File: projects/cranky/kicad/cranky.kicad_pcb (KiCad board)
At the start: 2 copper layers, 50 x 50 mm, 50 parts, among them CON1 USB-MINI-B, P1 ISP, P2 CONN_01X04, P3 CONN_01X04, P4 CONN_01X04, P5 CONN_01X04, Q1 2N7002P, Q2 2N7002P, Q3 ISL9V3040D3ST, Q4 ISL9V3040D3ST, Q5 VND5N07, Q6 VND5N07, SW1 SW_PUSH_SMALL, SW2 SW_PUSH_SMALL, U1 ATMEGA32U4-A, U2 LTV-826S, U3 LM7805CT, X1 16MHz

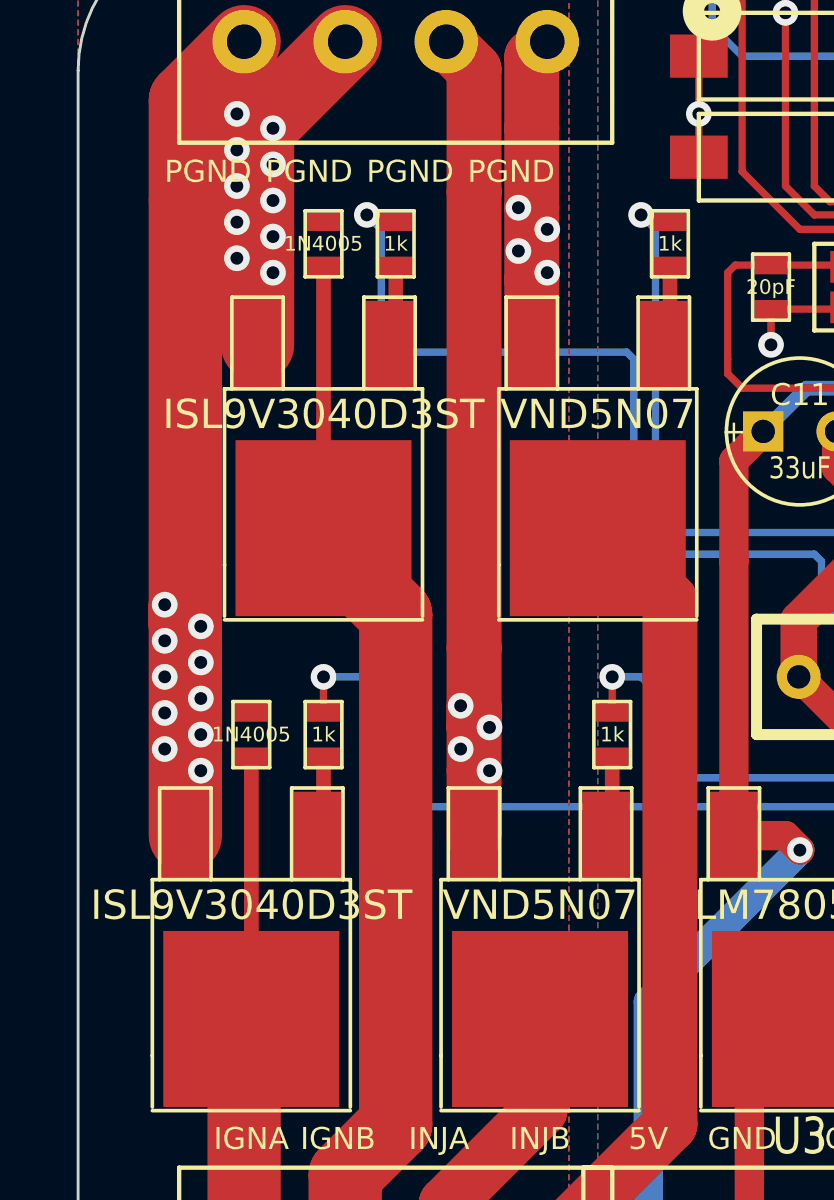
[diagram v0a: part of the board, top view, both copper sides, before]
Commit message: finished rerouting
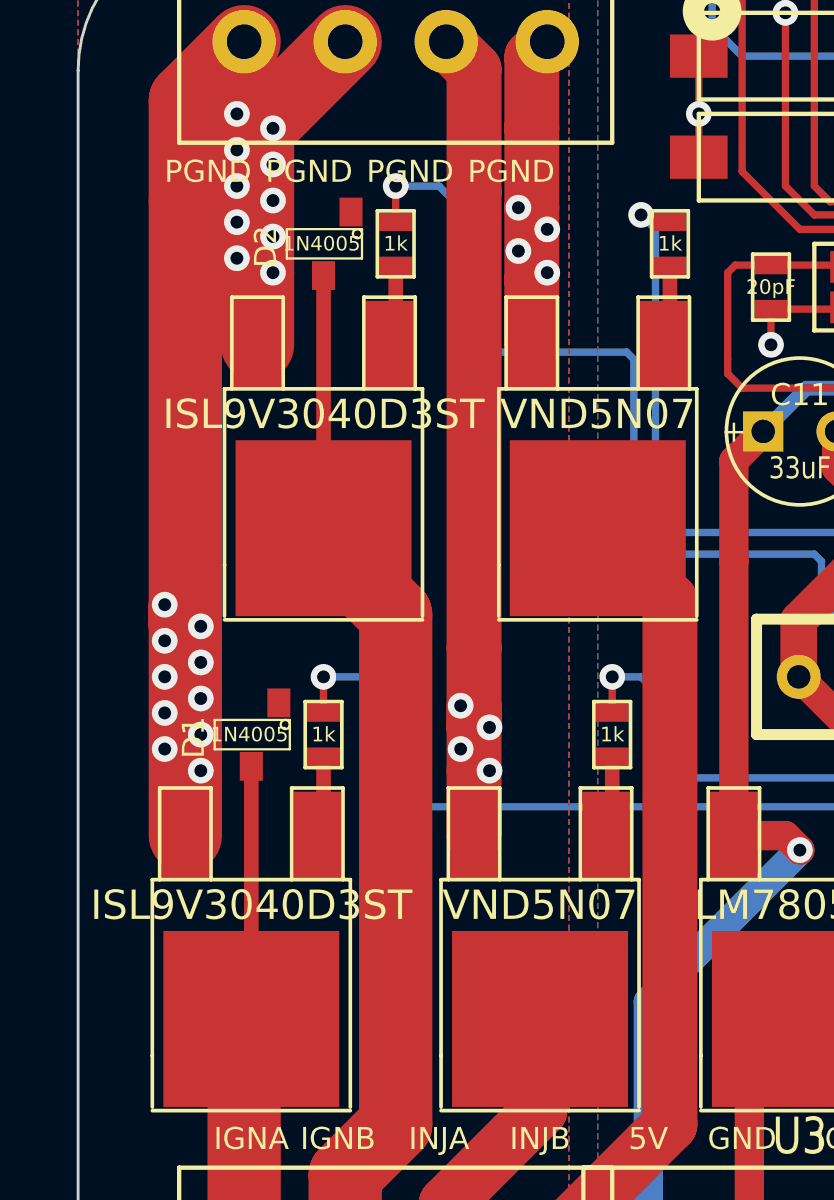
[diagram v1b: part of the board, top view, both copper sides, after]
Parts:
- D1, D2: footprint SM0603_VALUE -> SOT23
- turned D1 to 180 degrees
- turned D2 to 180 degrees
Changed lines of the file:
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@@
     (thickness 1.6)
     (drawings 27)
-    (tracks 482)
+    (tracks 483)
     (zones 0)
     (modules 50)
@@
     (19 F.Paste user)
     (20 B.SilkS user)
-    (21 F.SilkS user hide)
+    (21 F.SilkS user)
     (22 B.Mask user)
     (23 F.Mask user)
@@
     (mod_text_size 1 1)
     (mod_text_width 0.15)
-    (pad_size 6.096 6.096)
+    (pad_size 0.8001 1.00076)
     (pad_drill 0)
     (pad_to_mask_clearance 0)
@@
   )
   (module SM0603_VALUE (layer F.Cu)
-    (at 51 98 270)
-    (attr smd)
-    (fp_text reference D1 (at 0 0 270) (layer F.SilkS) hide
-      (effects (font (size 0.508 0.508) (thickness 0.1143)))
-    )
-    (fp_text value 1N4005 (at 0 0 360) (layer F.SilkS)
-      (effects (font (size 0.508 0.508) (thickness 0.1143)))
-    )
-    (fp_line (start -1.143 -0.635) (end 1.143 -0.635) (layer F.SilkS) (width 0.127))
-    (fp_line (start 1.143 -0.635) (end 1.143 0.635) (layer F.SilkS) (width 0.127))
-    (fp_line (start 1.143 0.635) (end -1.143 0.635) (layer F.SilkS) (width 0.127))
-    (fp_line (start -1.143 0.635) (end -1.143 -0.635) (layer F.SilkS) (width 0.127))
-    (pad 1 smd rect (at -0.762 0 270) (size 0.635 1.143)
-      (layers F.Cu F.Paste F.Mask)
-      (net 35 GNDPWR)
-    )
-    (pad 2 smd rect (at 0.762 0 270) (size 0.635 1.143)
-      (layers F.Cu F.Paste F.Mask)
-      (net 10 /IGNA)
-    )
-    (model smd\resistors\R0603.wrl
-      (at (xyz 0 0 0.001))
-      (scale (xyz 0.5 0.5 0.5))
-      (rotate (xyz 0 0 0))
-    )
-  )
-  (module SM0603_VALUE (layer F.Cu)
-    (at 53.5 81 270)
-    (attr smd)
-    (fp_text reference D2 (at 0 0 270) (layer F.SilkS) hide
-      (effects (font (size 0.508 0.508) (thickness 0.1143)))
-    )
-    (fp_text value 1N4005 (at 0 0 360) (layer F.SilkS)
-      (effects (font (size 0.508 0.508) (thickness 0.1143)))
-    )
-    (fp_line (start -1.143 -0.635) (end 1.143 -0.635) (layer F.SilkS) (width 0.127))
-    (fp_line (start 1.143 -0.635) (end 1.143 0.635) (layer F.SilkS) (width 0.127))
-    (fp_line (start 1.143 0.635) (end -1.143 0.635) (layer F.SilkS) (width 0.127))
-    (fp_line (start -1.143 0.635) (end -1.143 -0.635) (layer F.SilkS) (width 0.127))
-    (pad 1 smd rect (at -0.762 0 270) (size 0.635 1.143)
-      (layers F.Cu F.Paste F.Mask)
-      (net 35 GNDPWR)
-    )
-    (pad 2 smd rect (at 0.762 0 270) (size 0.635 1.143)
-      (layers F.Cu F.Paste F.Mask)
-      (net 11 /IGNB)
-    )
-    (model smd\resistors\R0603.wrl
-      (at (xyz 0 0 0.001))
-      (scale (xyz 0.5 0.5 0.5))
-      (rotate (xyz 0 0 0))
-    )
-  )
-  (module SM0603_VALUE (layer F.Cu)
     (at 53.5 98 90)
     (attr smd)
@@
       (scale (xyz 0.5 0.5 0.5))
       (rotate (xyz 0 0 0))
+    )
+  )
+  (module SOT23 (layer F.Cu)
+    (at 51 98 180)
+    (tags SOT23)
+    (fp_text reference D1 (at 1.99898 -0.09906 270) (layer F.SilkS)
+      (effects (font (size 0.762 0.762) (thickness 0.11938)))
+    )
+    (fp_text value 1N4005 (at 0.0635 0 180) (layer F.SilkS)
+      (effects (font (size 0.50038 0.50038) (thickness 0.09906)))
+    )
+    (fp_circle (center -1.17602 0.35052) (end -1.30048 0.44958) (layer F.SilkS) (width 0.07874))
+    (fp_line (start 1.27 -0.508) (end 1.27 0.508) (layer F.SilkS) (width 0.07874))
+    (fp_line (start -1.3335 -0.508) (end -1.3335 0.508) (layer F.SilkS) (width 0.07874))
+    (fp_line (start 1.27 0.508) (end -1.3335 0.508) (layer F.SilkS) (width 0.07874))
+    (fp_line (start -1.3335 -0.508) (end 1.27 -0.508) (layer F.SilkS) (width 0.07874))
+    (pad 2 smd rect (at 0 -1.09982 180) (size 0.8001 1.00076)
+      (layers F.Cu F.Paste F.Mask)
+      (net 10 /IGNA)
+    )
+    (pad 1 smd rect (at -0.9525 1.09982 180) (size 0.8001 1.00076)
+      (layers F.Cu F.Paste F.Mask)
+      (net 35 GNDPWR)
+    )
+    (model smd\SOT23_3.wrl
+      (at (xyz 0 0 0))
+      (scale (xyz 0.4 0.4 0.4))
+      (rotate (xyz 0 0 180))
+    )
+  )
+  (module SOT23 (layer F.Cu)
+    (at 53.5 81 180)
+    (tags SOT23)
+    (fp_text reference D2 (at 1.99898 -0.09906 270) (layer F.SilkS)
+      (effects (font (size 0.762 0.762) (thickness 0.11938)))
+    )
+    (fp_text value 1N4005 (at 0.0635 0 180) (layer F.SilkS)
+      (effects (font (size 0.50038 0.50038) (thickness 0.09906)))
+    )
+    (fp_circle (center -1.17602 0.35052) (end -1.30048 0.44958) (layer F.SilkS) (width 0.07874))
+    (fp_line (start 1.27 -0.508) (end 1.27 0.508) (layer F.SilkS) (width 0.07874))
+    (fp_line (start -1.3335 -0.508) (end -1.3335 0.508) (layer F.SilkS) (width 0.07874))
+    (fp_line (start 1.27 0.508) (end -1.3335 0.508) (layer F.SilkS) (width 0.07874))
+    (fp_line (start -1.3335 -0.508) (end 1.27 -0.508) (layer F.SilkS) (width 0.07874))
+    (pad 2 smd rect (at 0 -1.09982 180) (size 0.8001 1.00076)
+      (layers F.Cu F.Paste F.Mask)
+      (net 11 /IGNB)
+    )
+    (pad 1 smd rect (at -0.9525 1.09982 180) (size 0.8001 1.00076)
+      (layers F.Cu F.Paste F.Mask)
+      (net 35 GNDPWR)
+    )
+    (model smd\SOT23_3.wrl
+      (at (xyz 0 0 0))
+      (scale (xyz 0.4 0.4 0.4))
+      (rotate (xyz 0 0 180))
     )
   )
@@
   (segment (start 86.5 109.84982) (end 86.5 115.75) (width 0.254) (layer F.Cu) (net 9))
   (segment (start 86.5 115.75) (end 85.75 116.5) (width 0.254) (layer F.Cu) (net 9))
-  (segment (start 51 98.762) (end 51 107.85) (width 0.508) (layer F.Cu) (net 10))
+  (segment (start 51 99) (end 51 107.85) (width 0.508) (layer F.Cu) (net 10))
   (segment (start 50.75 116.5) (end 50.75 108.1) (width 2.54) (layer F.Cu) (net 10))
   (segment (start 50.75 108.1) (end 51 107.85) (width 2.54) (layer F.Cu) (net 10))
-  (segment (start 53.5 81.762) (end 53.5 90.85) (width 0.508) (layer F.Cu) (net 11))
+  (segment (start 53.5 82) (end 53.5 90.85) (width 0.508) (layer F.Cu) (net 11))
   (segment (start 54.25 116.5) (end 54.25 113.25) (width 2.54) (layer F.Cu) (net 11))
   (segment (start 56 93.85) (end 53 90.85) (width 2.54) (layer F.Cu) (net 11))
@@
   (segment (start 56 100.5) (end 55.5 100) (width 0.254) (layer B.Cu) (net 19))
   (segment (start 82 100.5) (end 56 100.5) (width 0.254) (layer B.Cu) (net 19))
+  (segment (start 57.5 79) (end 56 79) (width 0.254) (layer B.Cu) (net 20))
+  (segment (start 56 79) (end 56 80.238) (width 0.254) (layer F.Cu) (net 20))
+  (via (at 56 79) (size 0.889) (layers F.Cu B.Cu) (net 20))
+  (segment (start 58.5 84.75) (end 58.25 84.75) (width 0.254) (layer B.Cu) (net 20))
+  (segment (start 58 79.5) (end 57.5 79) (width 0.254) (layer B.Cu) (net 20))
+  (segment (start 58 84.5) (end 58 79.5) (width 0.254) (layer B.Cu) (net 20))
+  (segment (start 58.25 84.75) (end 58 84.5) (width 0.254) (layer B.Cu) (net 20))
   (segment (start 85.8001 94.715) (end 85.8001 91.8001) (width 0.254) (layer F.Cu) (net 20))
   (segment (start 85.5 91.5) (end 82 91.5) (width 0.254) (layer B.Cu) (net 20))
   (via (at 85.5 91.5) (size 0.889) (layers F.Cu B.Cu) (net 20))
   (segment (start 85.8001 91.8001) (end 85.5 91.5) (width 0.254) (layer F.Cu) (net 20))
-  (segment (start 55.5 80.5) (end 55.5 84.5) (width 0.254) (layer B.Cu) (net 20))
   (segment (start 70.75 93.5) (end 71.25 94) (width 0.254) (layer B.Cu) (net 20))
   (segment (start 70.75 92) (end 70.75 93.5) (width 0.254) (layer B.Cu) (net 20))
@@
   (segment (start 64.25 85) (end 64.25 90.75) (width 0.254) (layer B.Cu) (net 20))
   (segment (start 64 84.75) (end 64.25 85) (width 0.254) (layer B.Cu) (net 20))
-  (segment (start 55.75 84.75) (end 64 84.75) (width 0.254) (layer B.Cu) (net 20))
-  (segment (start 55.5 84.5) (end 55.75 84.75) (width 0.254) (layer B.Cu) (net 20))
+  (segment (start 58.5 84.75) (end 64 84.75) (width 0.254) (layer B.Cu) (net 20))
   (segment (start 79.5 94) (end 71.25 94) (width 0.254) (layer B.Cu) (net 20))
   (segment (start 80.5 93) (end 79.5 94) (width 0.254) (layer B.Cu) (net 20))
   (segment (start 82 91.5) (end 80.5 93) (width 0.254) (layer B.Cu) (net 20))
-  (segment (start 55.238 80.238) (end 56 80.238) (width 0.254) (layer F.Cu) (net 20))
-  (segment (start 55 80) (end 55.238 80.238) (width 0.254) (layer F.Cu) (net 20))
-  (via (at 55 80) (size 0.889) (layers F.Cu B.Cu) (net 20))
-  (segment (start 55.5 80.5) (end 55 80) (width 0.254) (layer B.Cu) (net 20))
   (segment (start 87.262 105.25) (end 87.262 104.488) (width 0.254) (layer F.Cu) (net 21))
   (segment (start 87.5 96.25) (end 87.4003 96.1503) (width 0.254) (layer F.Cu) (net 21))

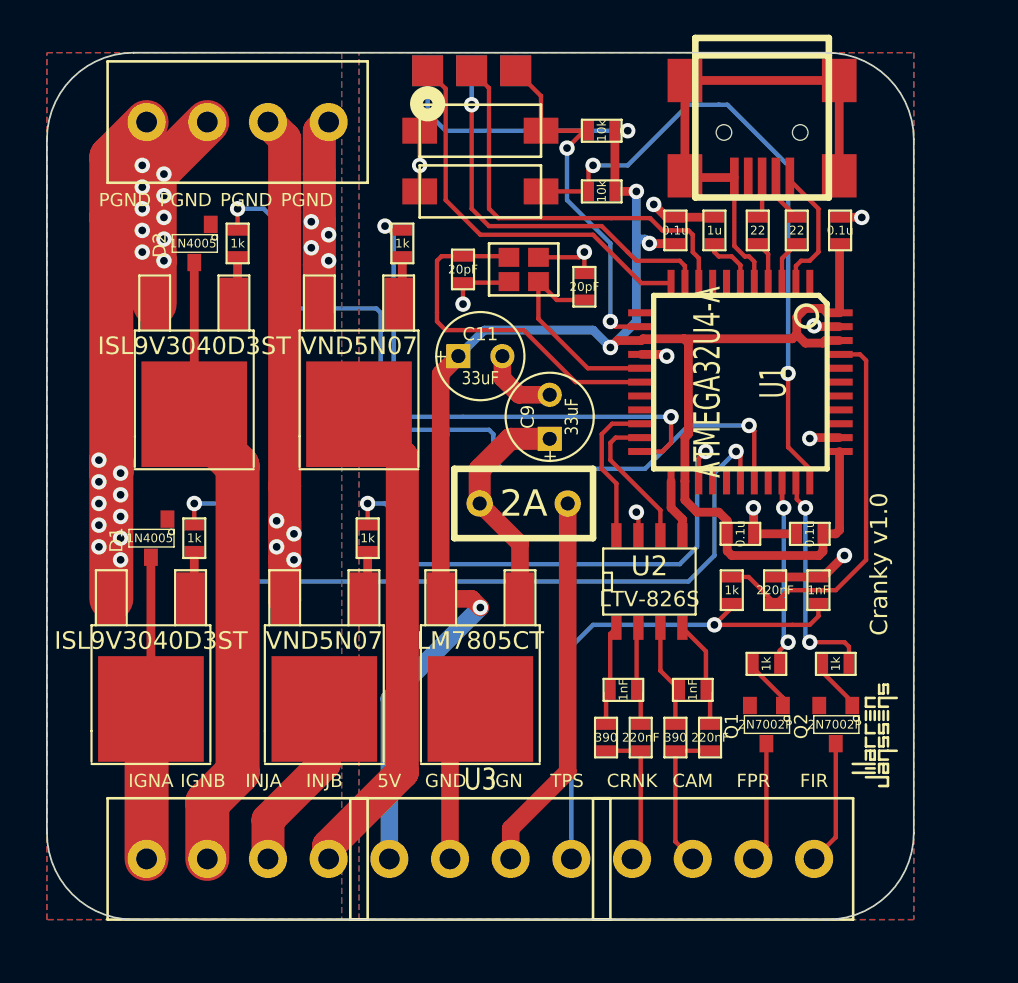
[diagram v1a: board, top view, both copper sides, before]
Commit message: adding zones for igbts
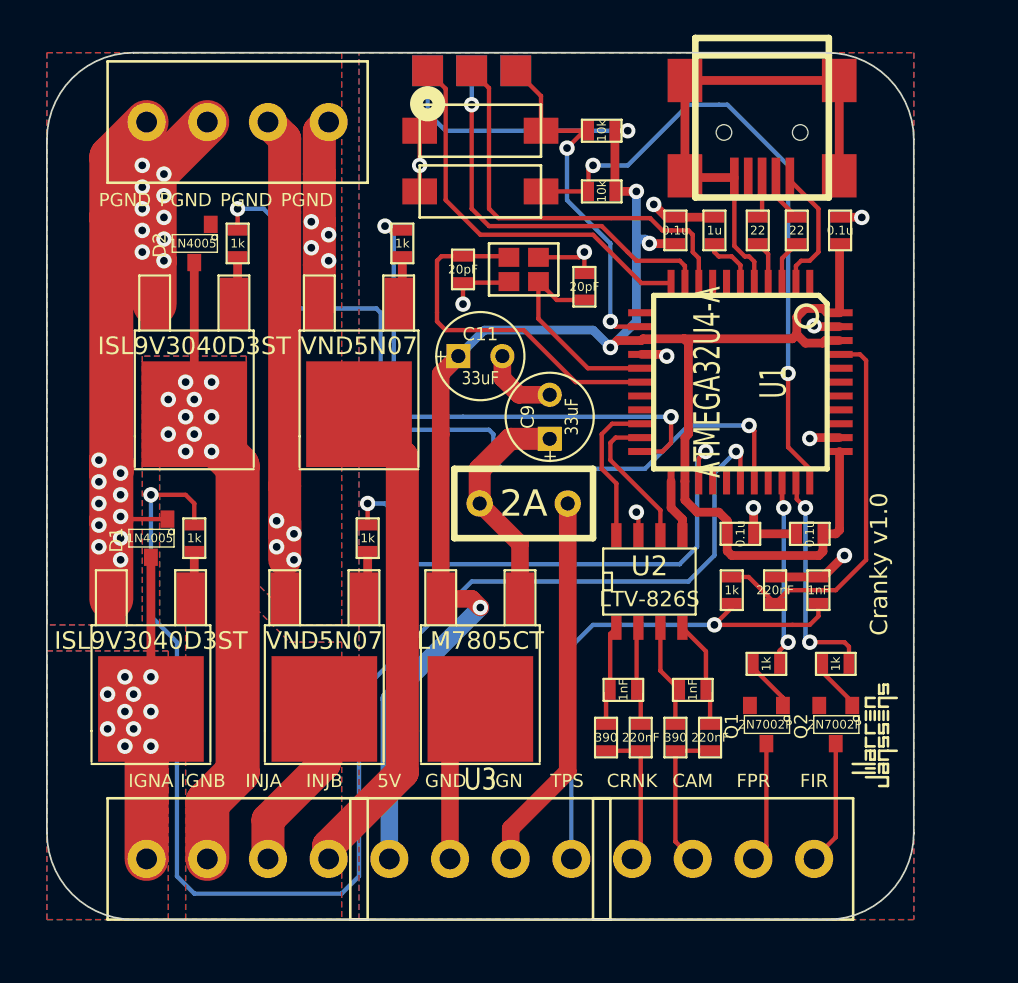
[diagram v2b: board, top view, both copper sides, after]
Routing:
- net /PB4: track 44.1 -> 80.5 mm
- net /IGNB: track 36.5 -> 52.0 mm, vias 0 -> 10
- net /IGNA: track 17.6 -> 32.8 mm, vias 0 -> 10
- net GNDPWR: track 122.1 -> 125.8 mm
- added copper zone on B.Cu, net /IGNA
- added copper zone on F.Cu, net /IGNA
- added copper zone on B.Cu, net /IGNB
- added copper zone on F.Cu, net /IGNB

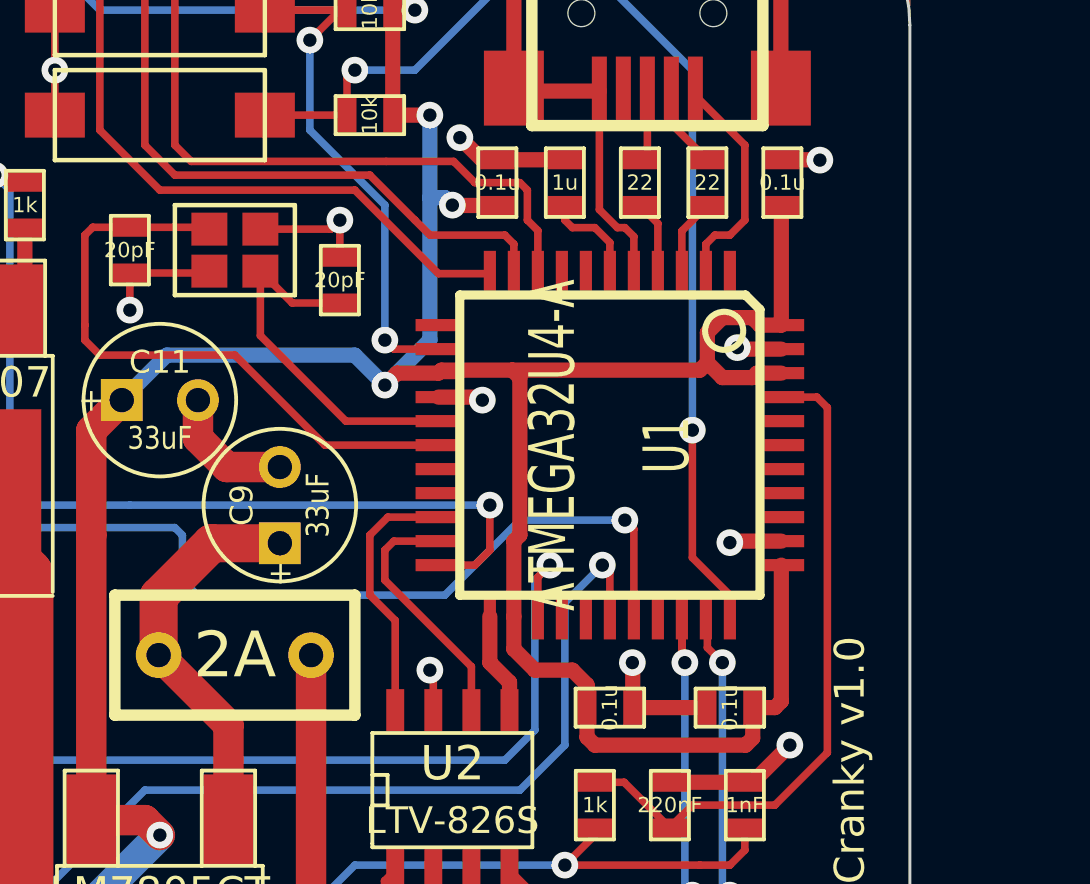
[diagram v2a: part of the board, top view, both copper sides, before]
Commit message: adding missing cap on aref
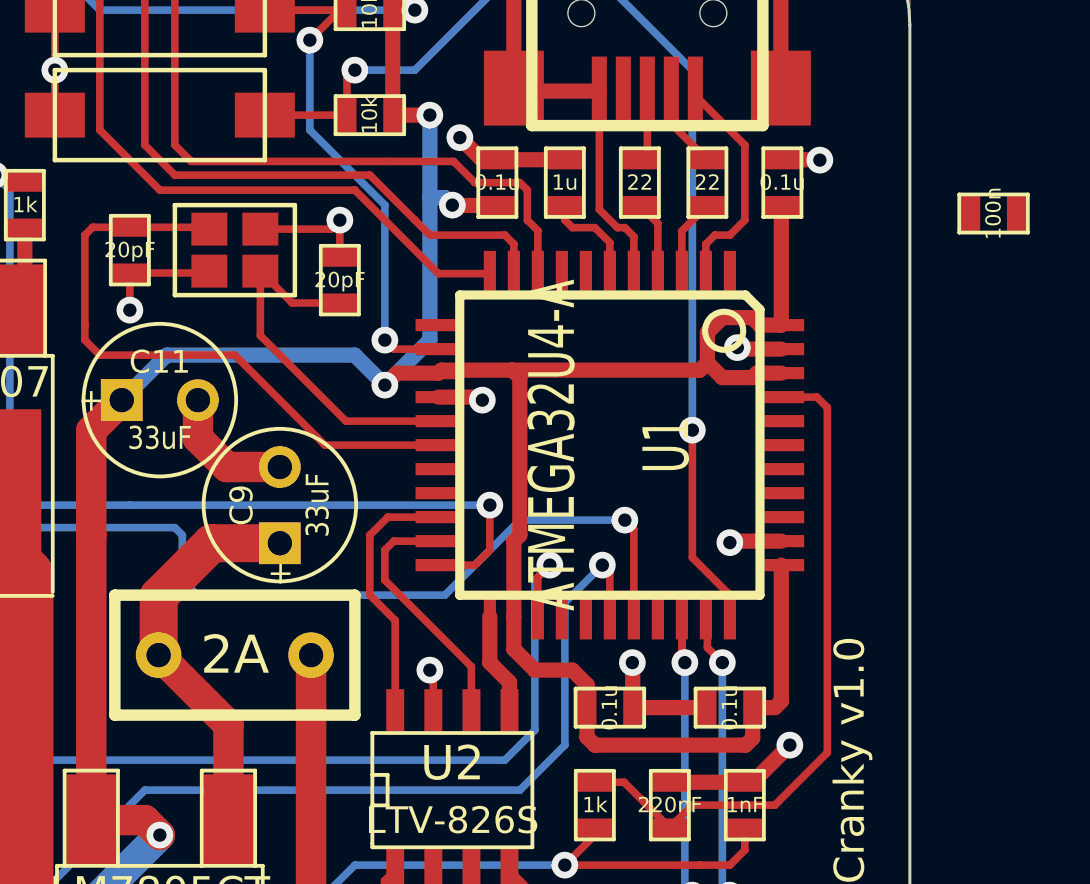
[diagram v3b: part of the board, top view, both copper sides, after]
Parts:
- added C16: 100n, custom:SM0603_VALUE, F.Cu at (97.8, 81.3)
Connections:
- CON1 pad 1: /UVCC -> Net-(CON1-Pad1)
- CON1 pad 2: /UDM -> Net-(CON1-Pad2)
- CON1 pad 3: /UDP -> Net-(CON1-Pad3)
- CON1 pad 4: (no net) -> Net-(CON1-Pad4)
- CON1 pad 5: /UGND -> Net-(CON1-Pad5)
- CON1 pad 6: /UGND -> Net-(CON1-Pad6)
- CON1 pad 7: /UGND -> Net-(CON1-Pad7)
- CON1 pad 8: /UGND -> Net-(CON1-Pad8)
- CON1 pad 9: /UGND -> Net-(CON1-Pad9)
- U1 pad 1: (no net) -> Net-(U1-Pad1)
- U1 pad 12: (no net) -> Net-(U1-Pad12)
- U1 pad 18: (no net) -> Net-(U1-Pad18)
- U1 pad 19: (no net) -> Net-(U1-Pad19)
- U1 pad 26: (no net) -> Net-(U1-Pad26)
- U1 pad 27: (no net) -> Net-(U1-Pad27)
- U1 pad 30: (no net) -> Net-(U1-Pad30)
- U1 pad 36: (no net) -> Net-(U1-Pad36)
- U1 pad 37: (no net) -> Net-(U1-Pad37)
- U1 pad 38: (no net) -> Net-(U1-Pad38)
- U1 pad 39: (no net) -> Net-(U1-Pad39)
- U1 pad 40: (no net) -> Net-(U1-Pad40)
- U1 pad 42: VCC -> Net-(C16-Pad2)
- U1 pad 7: (no net) -> /VBUS
- U1 pad 8: (no net) -> Net-(U1-Pad8)
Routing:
- net /UGND: track 29.5 -> 2.76 mm
- net Net-(CON1-Pad9): track 0.00 -> 14.4 mm
- net Net-(CON1-Pad7): track 0.00 -> 5.50 mm
- net Net-(C16-Pad2): track 0.00 -> 4.44 mm
- net VCC: track 123.4 -> 118.9 mm
- net Net-(CON1-Pad5): track 0.00 -> 3.95 mm
- net Net-(CON1-Pad8): track 0.00 -> 2.89 mm
- net Net-(CON1-Pad2): track 0.00 -> 2.79 mm
- net /UDM: track 2.79 -> 0.00 mm
- net /UVCC: track 7.60 -> 5.12 mm
- net Net-(CON1-Pad1): track 0.00 -> 2.48 mm
